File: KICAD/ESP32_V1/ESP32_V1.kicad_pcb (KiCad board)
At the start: 2 copper layers, 90.1 x 70 mm, 36 parts

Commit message: Align ESP32 V1 PCB guide grid and placement
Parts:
- moved J_ADC_Header1 4.49 mm to (88.7, 66.0)
- moved R7 4.21 mm to (116.6, 68.6)
- moved R3 4.14 mm to (116.6, 91.4)
- moved R4 4.14 mm to (116.6, 99.0)
- moved R5 4.14 mm to (116.6, 106.7)
- moved R6 4.14 mm to (116.6, 76.2)
- moved R2 4.14 mm to (116.6, 83.9)
- moved U_SPI1 4.14 mm to (93.7, 66.0)
- moved MH4 2.54 mm to (74.6, 112.5)
- moved J_Grove_I2C1 2.44 mm to (78.5, 93.9)
- moved SEL_D26 1.98 mm to (106.4, 99.4)
- moved J_FLASH1 1.95 mm to (78.5, 66.0)
- moved SEL_D33 1.95 mm to (106.4, 71.1)
- moved JP_UART_LOOP2 1.67 mm to (111.5, 50.8)
- moved R12 1.65 mm to (106.4, 88.9)
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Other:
- board size 90.1 x 70 mm -> 90 x 70 mm
- board text added: "Espruino ESP32 DevKitC V4 Test Harness"
- board text added: "SimonGAndrews Rev 1.0"

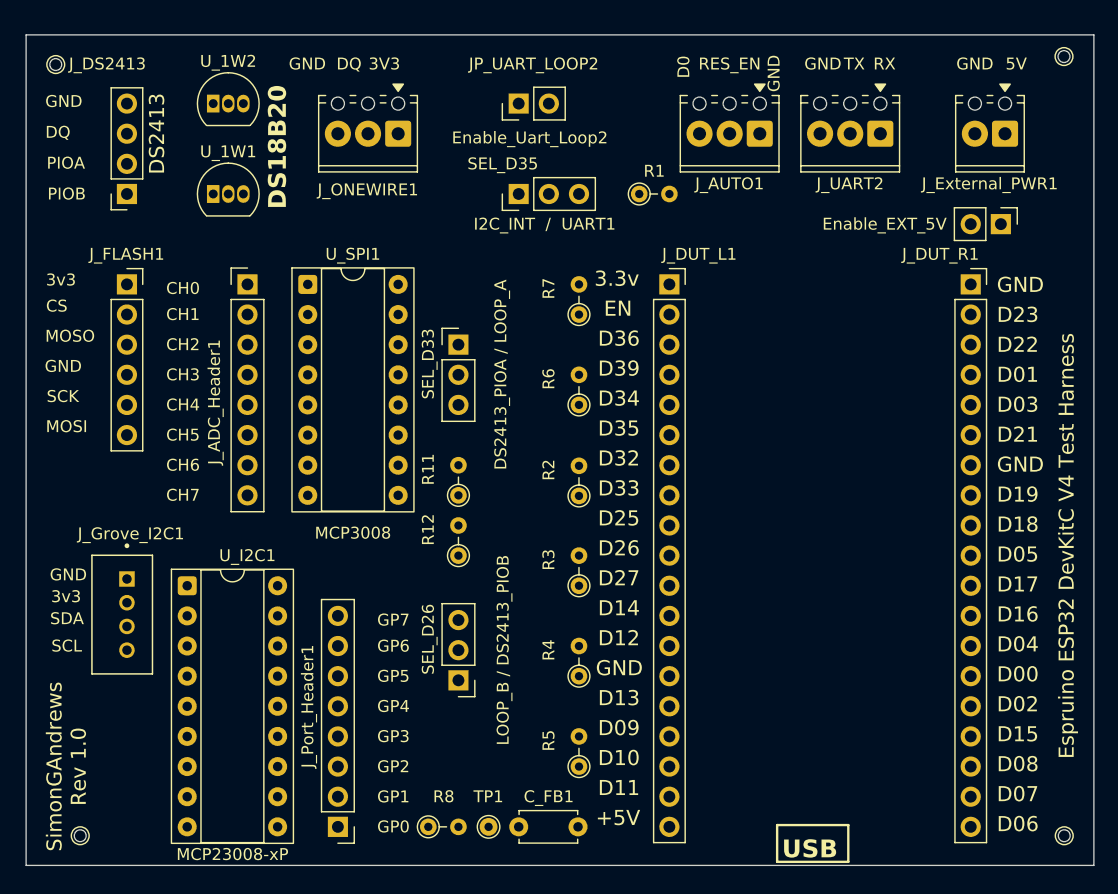
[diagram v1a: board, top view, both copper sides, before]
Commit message: Finalize ESP32_V1 v1.0 build documentation
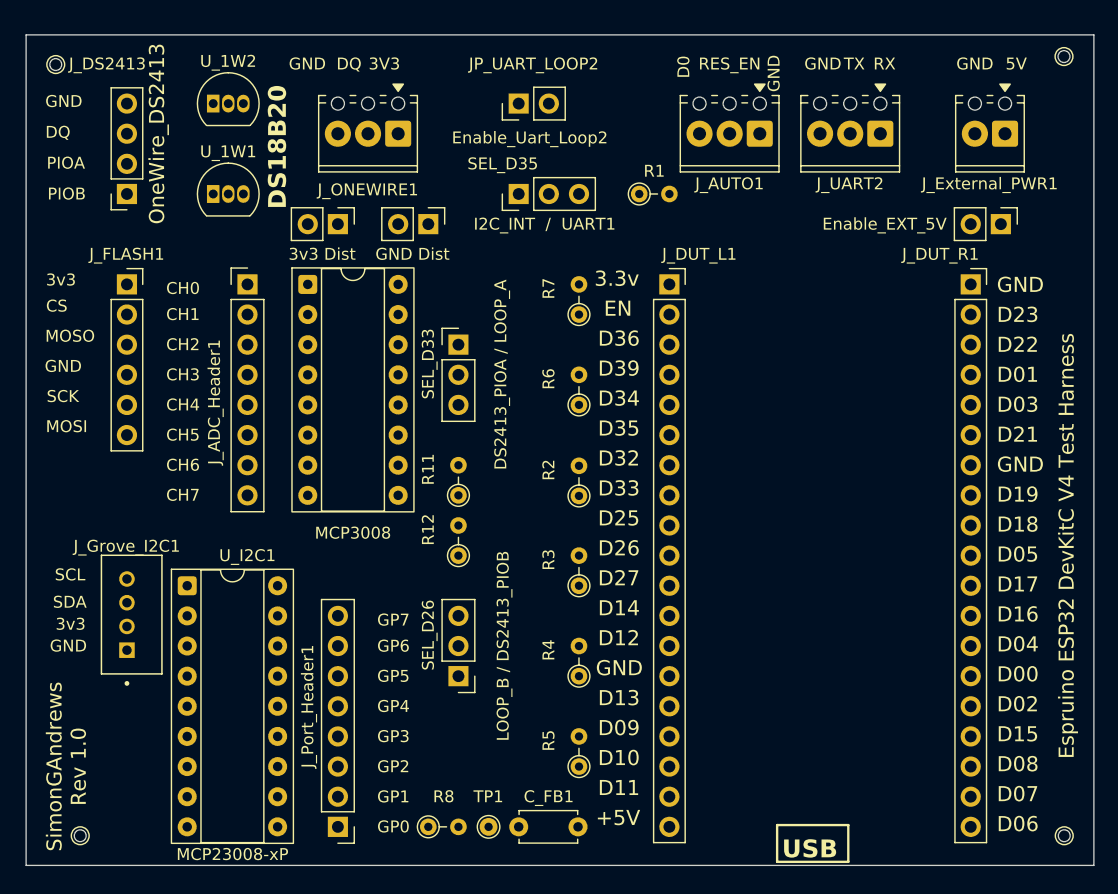
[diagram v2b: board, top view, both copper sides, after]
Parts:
- added J1: 3v3 Dist, ESP32_V1:PinHeader_1x02_P2.54mm_Vertical, F.Cu at (96.3, 61.0)
- added J2: GND Dist, ESP32_V1:PinHeader_1x02_P2.54mm_Vertical, F.Cu at (103.9, 61.0)
- R6: value 2K2 -> 2K
- moved SEL_D26 0.35 mm to (106.4, 99.0)
- turned J_Grove_I2C1 to 90 degrees
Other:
- board text added: "3v3 Dist"
- board text added: "GND Dist"
